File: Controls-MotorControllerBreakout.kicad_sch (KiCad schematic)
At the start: 12 parts, among them J1 MC CAN 1, J2 MC CAN 2, J3 CTRLS, J4 EXT PWR, J5 CANDAPTER

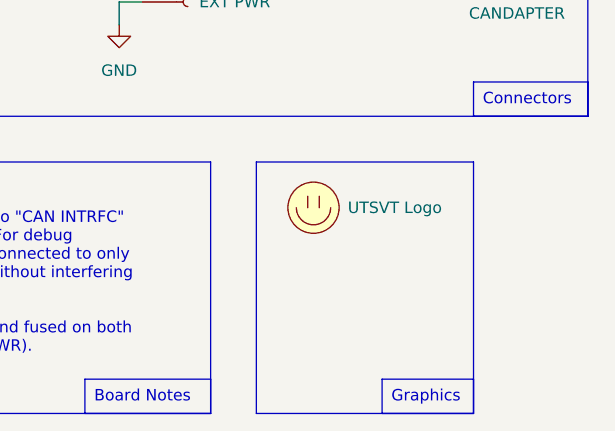
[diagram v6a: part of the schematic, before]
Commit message: mc interface footprint & better input pours
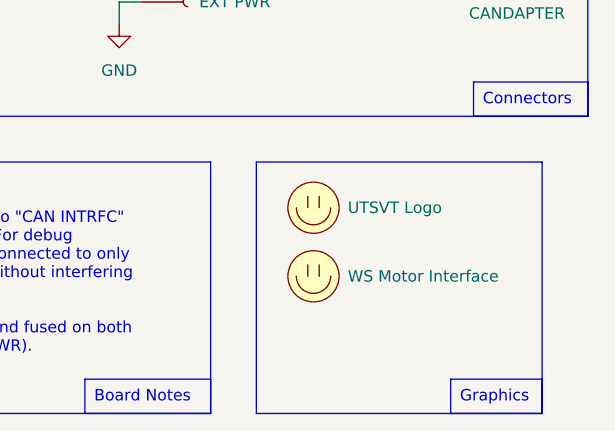
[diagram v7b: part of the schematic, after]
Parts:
- added LOGO2: WS Motor Interface, Wavesculptor_Motor_Interface:Wavesculptor_Motor_Interface_Type_1, symbol utsvt-misc:Logo_Placeholder
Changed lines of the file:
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@@
 	(rectangle
 		(start 140.97 73.66)
-		(end 165.1 101.6)
+		(end 172.72 101.6)
 		(stroke
 			(width 0)
@@
 	(text_box "Graphics"
 		(exclude_from_sim no)
-		(at 154.94 97.79 0)
+		(at 162.56 97.79 0)
 		(size 10.16 3.81)
 		(stroke
@@
 					(unit 1)
 				)
+			)
+		)
+	)
+	(symbol
+		(lib_id "utsvt-misc:Logo_Placeholder")
+		(at 147.32 86.36 0)
+		(unit 1)
+		(exclude_from_sim no)
+		(in_bom yes)
+		(on_board yes)
+		(dnp no)
+		(fields_autoplaced yes)
+		(property "Reference" "LOGO2"
+			(at 147.32 82.55 0)
+			(effects
+				(font
+					(size 1.27 1.27)
+				)
+				(hide yes)
+			)
+		)
+		(property "Value" "WS Motor Interface"
+			(at 151.13 86.3599 0)
+			(effects
+				(font
+					(size 1.27 1.27)
+				)
+				(justify left)
+			)
+		)
+		(property "Footprint" "Wavesculptor_Motor_Interface:Wavesculptor_Motor_Interface_Type_1"
+			(at 147.32 84.455 0)
+			(effects
+				(font
+					(size 1.27 1.27)
+				)
+				(hide yes)
+			)
+		)
+		(property "Datasheet" ""
+			(at 147.32 84.455 0)
+			(effects
+				(font
+					(size 1.27 1.27)
+				)
+				(hide yes)
+			)
+		)
+		(property "Description" "Graph footprint placeholder"
+			(at 147.32 86.36 0)
+			(effects
+				(font
+					(size 1.27 1.27)
+				)
+				(hide yes)
+			)
+		)
+		(property "Sim.Device" ""
+			(at 147.32 86.36 0)
+			(effects
+				(font
+					(size 1.27 1.27)
+				)
+				(hide yes)
+			)
+		)
+		(property "Sim.Pins" ""
+			(at 147.32 86.36 0)
+			(effects
+				(font
+					(size 1.27 1.27)
+				)
+				(hide yes)
+			)
+		)
+		(instances
+			(project "Controls-MotorControllerBreakout"
+				(path "/0a971d65-5373-49c6-bc07-3a5d4263dbef"
+					(reference "LOGO2")
+					(unit 1)
+				)

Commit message: yap
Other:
- note added: "This board allows for easier debugging of the WaveSculptor motor controller by switching between controls and external power sources and providing a plug-and-play CANdapter interface. Controls Leader should always be connected to "CTRLS" with the standard CAN+PWR pinout. Motor controller should always be connected to MC CAN 1 and MC CAN 2. To connect external 12V power, the "EXT EN" jumper must b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"
- note removed: "THIS IS WRONG! UPDATE! Controls Leader should be connected to "CAN INTRFC" and "EXT PWR" for normal operation. For debug purposes, Controls Leader should be connected to only "EXT PWR" to provide 12v to the MC without interfering with Profinity controls software. +12v is protected by rectifier diodes and fused on both Controls Leader and this board (EXT PWR)."
- note removed: "TODO: add testpoints and stuff"
- moved on the sheet: H1, H2, H3, H4, J1, J2, J3, J4, J5, JP1, R1
